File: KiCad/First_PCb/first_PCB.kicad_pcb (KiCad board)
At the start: 2 copper layers, 120 x 120 mm, 41 parts, among them J1 Conn_01x04_Socket, J2 Conn_01x04_Socket, J3 Conn_01x04_Socket, J4 Conn_01x02_Pin, J5 DC-005, U1 MT3608 TYPE-C USB, U2 GH1.25, U3 STEVAL-MKI239A, U4 EGBO UPS, U5 ESP32-DEVKITC-32D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

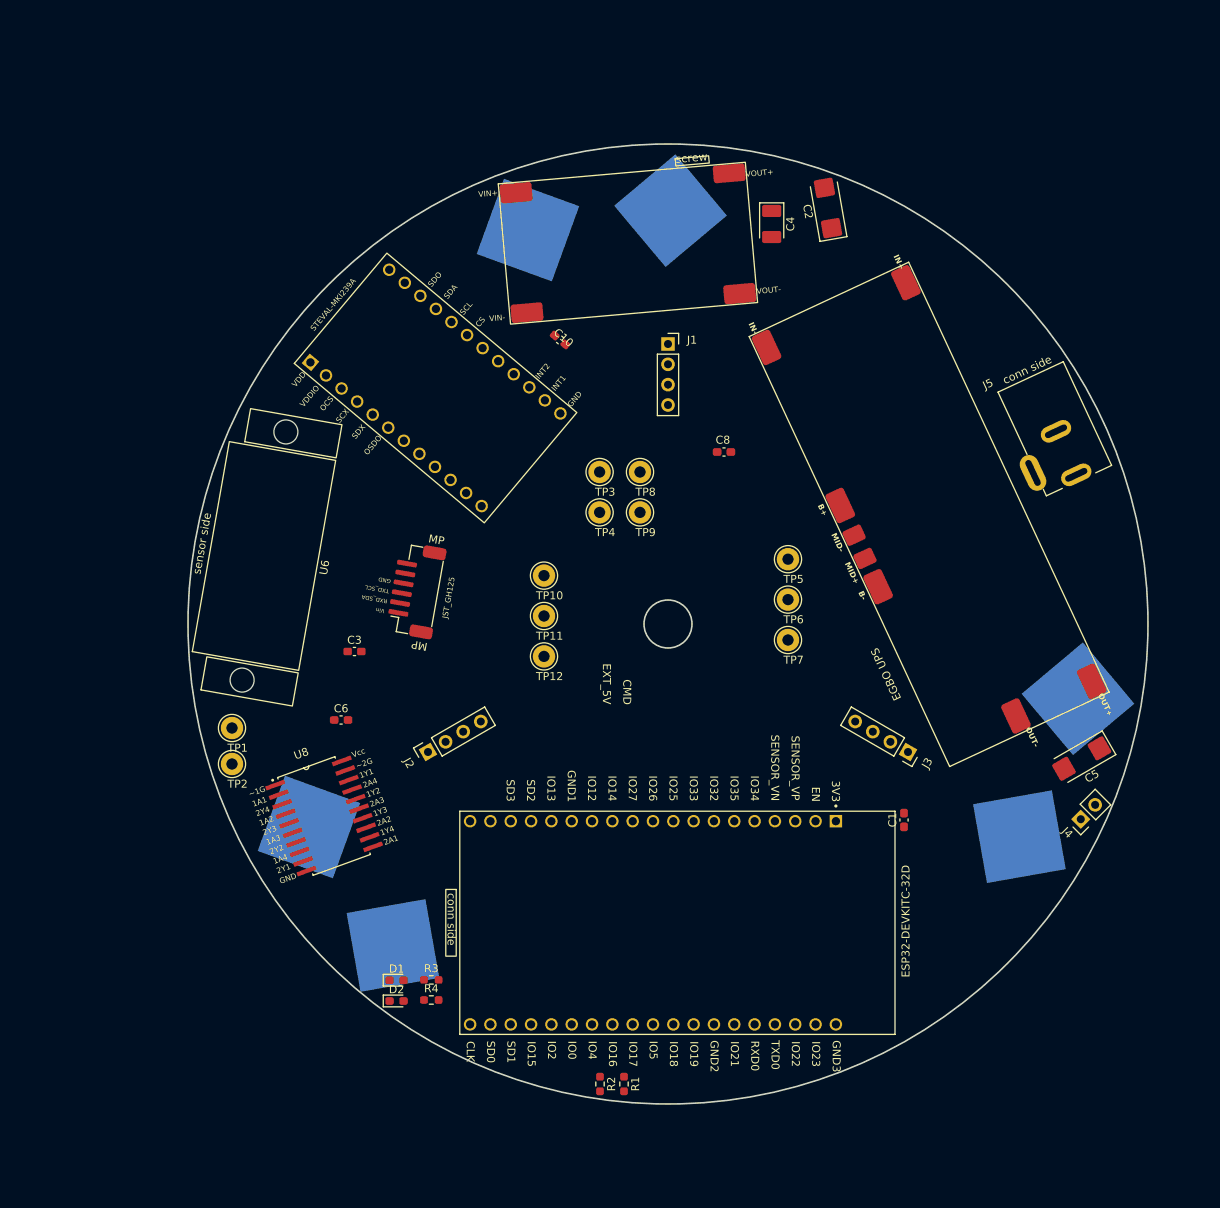
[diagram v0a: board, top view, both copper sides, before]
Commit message: added all the kicad files & gerbers of the first pcb
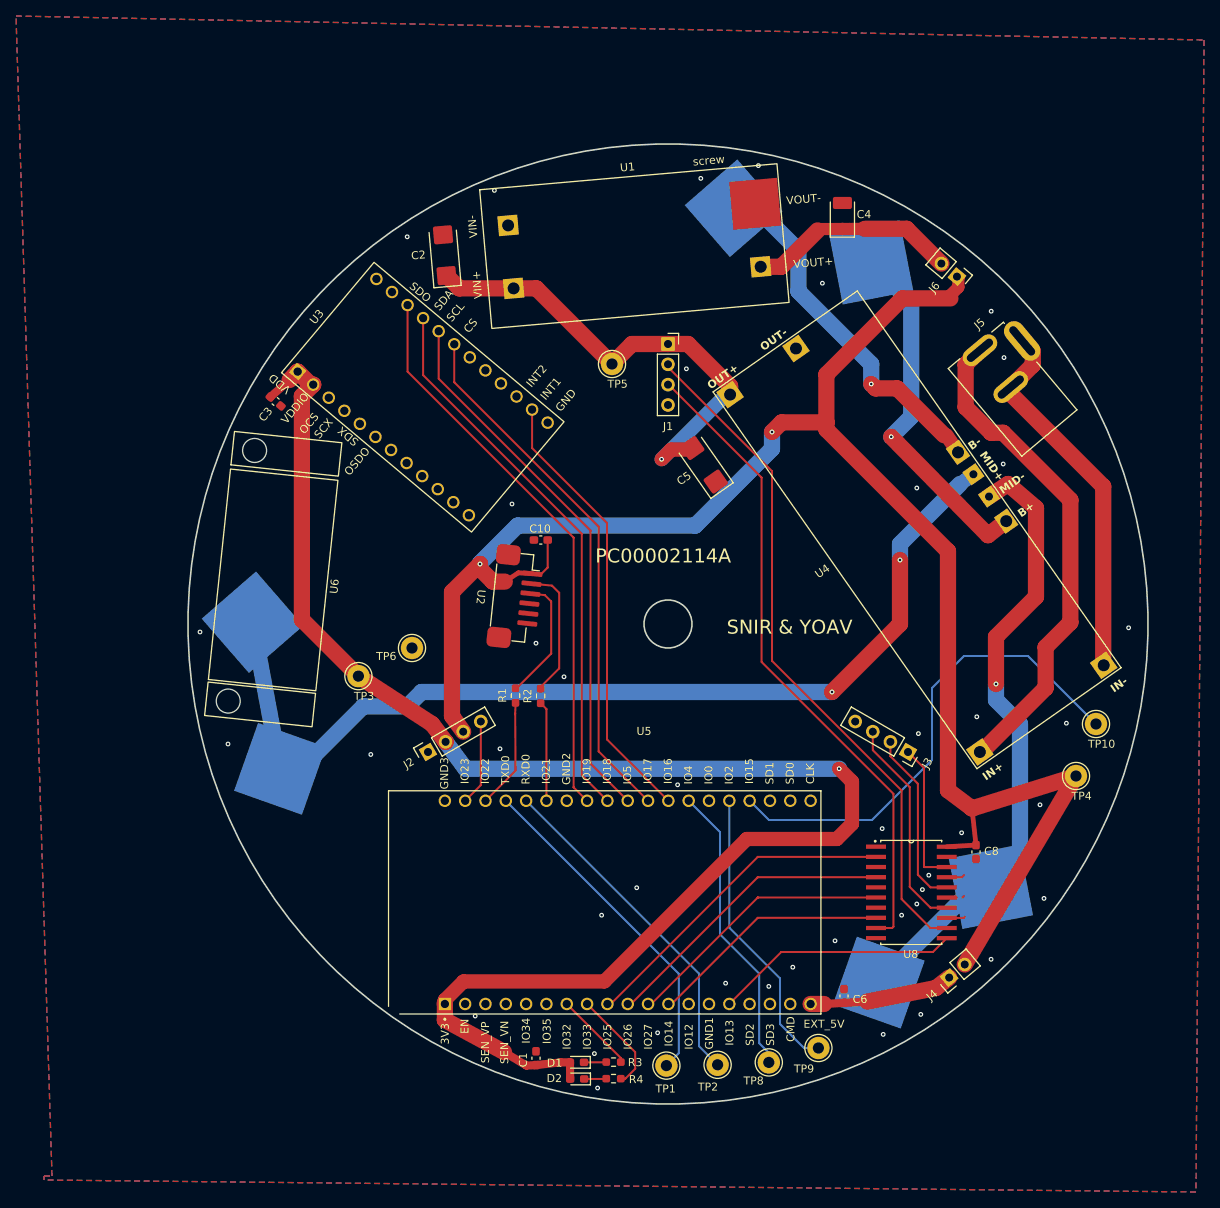
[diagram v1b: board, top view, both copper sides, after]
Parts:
- removed TP11, TP12, TP7: TestPoint, TestPoint:TestPoint_Loop_D2.60mm_Drill1.4mm_Beaded
- added J6: Conn_01x02_Pin, Connector_PinHeader_2.54mm:PinHeader_1x02_P2.54mm_Vertical, F.Cu at (136.1, 56.6)
- U1: value MT3608 TYPE-C USB -> MT3608 - No Connector; footprint footprints:MT3608 Type-C USB -> footprints:MT3608_no_conn_TH
- U4: footprint footprints:PWR_SPLY12V -> footprints:PWR_SPLY12V_TH
- moved TP8 75.5 mm to (112.6, 154.8)
- moved U8 74.0 mm to (130.4, 133.6), turned to 0 degrees
- moved C6 71.7 mm to (122.0, 146.5), turned to 90 degrees
- moved TP10 71.5 mm to (153.5, 112.5)
- moved TP2 71.4 mm to (106.2, 155.1)
- moved TP9 70.6 mm to (118.8, 153.0)
- moved TP1 68.8 mm to (99.8, 155.2)
- moved TP4 68.1 mm to (151.0, 119.0)
- moved C5 59.8 mm to (104.5, 80.1), turned to 125 degrees
- moved C8 59.1 mm to (138.5, 128.5), turned to -90 degrees
- moved C1 54.8 mm to (83.5, 154.3)
- moved R1 50.4 mm to (80.9, 109.0), turned to 90 degrees
- moved R2 49.1 mm to (84.1, 109.0), turned to 90 degrees
- moved C2 48.3 mm to (72.1, 53.9), turned to 95 degrees
- moved TP6 47.4 mm to (68.0, 103.0)
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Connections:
- BT1 pad N: Net-(U4-MID+) -> Net-(U4-B-)
- BT1 pad P: Net-(U4-B+) -> Net-(U4-MID-)
- BT2 pad N: Net-(U4-MID-) -> Net-(U4-MID+)
- BT2 pad P: Net-(U4-MID+) -> Net-(U4-B+)
- BT3 pad N: Net-(U4-B-) -> Net-(U4-MID-)
- BT3 pad P: Net-(U4-MID-) -> Net-(U4-MID+)
- C4 pad 1: +5V -> Net-(J6-Pin_2)
- C6 pad 1: +5V -> Net-(J4-Pin_1)
- J1 pad 1: /Processing/ESP_LEDS_CLK -> +12V
- J1 pad 2: /Processing/ESP_LEDS_SDI1 -> /Processing/ESP_LEDS_SDI4
- J1 pad 3: +3.3V -> /Processing/ESP_LEDS_CLK
- J2 pad 1: /Processing/ESP_2ND_PCB_GPIO4 -> GND
- J2 pad 2: /Processing/ESP_LEDS_SDI2 -> +3.3V
- J2 pad 4: GND -> /Processing/ESP_2ND_PCB_GPIO23
- J3 pad 1: /Processing/ESP_LEDS_SDI4 -> /Processing/ESP_LEDS_SDI1
- J3 pad 2: /Processing/ESP_LEDS_SDI3 -> /Processing/ESP_LEDS_SDI2
- J3 pad 3: +12V -> /Processing/ESP_LEDS_SDI3
- R1 pad 1: Net-(U5-IO17) -> Net-(U5-IO22)
- R1 pad 2: /Processing/ESP_LUNA_UART_TX -> /Processing/ESP_LUNA_UART_RX
- R2 pad 1: Net-(U5-IO16) -> Net-(U5-IO21)
- R2 pad 2: /Processing/ESP_LUNA_UART_RX -> /Processing/ESP_LUNA_UART_TX
- R4 pad 1: /Display/ESP_ST_LED2 -> /Processing/ESP_ST_LED2
- TP10 pad 1: /Processing/ESP_first_PCB_GPIO2 -> /Processing/ESP_TP_GPIO15
- TP8 pad 1: /Test Pins/ESP_first_PCB_GPIO22 -> /Test Pins/ESP_TP_GPIO4
- TP9 pad 1: /Processing/ESP_first_PCB_GPIO15 -> /Processing/ESP_TP_GPIO2
- U1 pad 3: +5V -> Net-(J6-Pin_2)
- U5 pad J2-10: /Processing/ESP_LEDS_SDI4_3.3v -> /Processing/ESP_LEDS_SDI2_3.3v
- U5 pad J2-12: /Processing/ESP_LEDS_SDI2_3.3v -> /Processing/ESP_LEDS_SDI4_3.3v
- U5 pad J2-15: /Processing/ESP_LEDS_SDI1_3.3v -> /Processing/ESP_LEDS_CLK_3.3v
- U5 pad J2-5: /Processing/ESP_first_PCB_GPIO34 -> unconnected-(U5-IO34-PadJ2-5)
- U5 pad J2-6: /Processing/ESP_first_PCB_GPIO35 -> unconnected-(U5-IO35-PadJ2-6)
- U5 pad J2-7: /Processing/JYRO_ESP_INT1 -> /Processing/ESP_ST_LED1
- U5 pad J2-8: /Processing/ESP_ST_LED1 -> /Processing/ESP_ST_LED2
- U5 pad J2-9: /Processing/ESP_LEDS_CLK_3.3v -> /Processing/ESP_LEDS_SDI1_3.3v
- U5 pad J3-10: /Processing/ESP_JYRO_SPI_CS -> /Processing/ESP_JYRO_SPI_CLK
- U5 pad J3-11: Net-(U5-IO17) -> /Processing/ESP_JYRO_SPI_CS
- U5 pad J3-12: Net-(U5-IO16) -> /Processing/JYRO_ESP_INT1
- U5 pad J3-13: /Processing/ESP_2ND_PCB_GPIO4 -> /Test Pins/ESP_TP_GPIO4
- U5 pad J3-15: /Processing/ESP_first_PCB_GPIO2 -> /Processing/ESP_TP_GPIO2
- U5 pad J3-16: /Processing/ESP_first_PCB_GPIO15 -> /Processing/ESP_TP_GPIO15
- U5 pad J3-2: /Processing/ESP_JYRO_SPI_MOSI -> /Processing/ESP_2ND_PCB_GPIO23
- U5 pad J3-3: /Test Pins/ESP_first_PCB_GPIO22 -> Net-(U5-IO22)
- U5 pad J3-6: /Display/ESP_ST_LED2 -> Net-(U5-IO21)
- U5 pad J3-9: /Processing/ESP_JYRO_SPI_CLK -> /Processing/ESP_JYRO_SPI_MOSI
- U8 pad 13: unconnected-(U8-2A2-Pad13) -> GND
- U8 pad 15: unconnected-(U8-2A3-Pad15) -> GND
- U8 pad 17: unconnected-(U8-2A4-Pad17) -> GND
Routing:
- net +5V: track 0.00 -> 222.5 mm, vias 0 -> 2
- net +3.3V: track 0.00 -> 201.4 mm, vias 0 -> 1
- net Net-(U4-MID-): track 0.00 -> 126.3 mm, vias 0 -> 2
- net /Processing/ESP_LEDS_SDI4: track 0.00 -> 87.2 mm
- net /Processing/ESP_LEDS_CLK: track 0.00 -> 81.7 mm
- net Net-(U4-MID+): track 0.00 -> 78.6 mm, vias 0 -> 1
- net /Processing/ESP_JYRO_SPI_MISO: track 0.00 -> 71.4 mm
- net /Processing/ESP_JYRO_SPI_MOSI: track 0.00 -> 69.9 mm
- net /Processing/ESP_JYRO_SPI_CLK: track 0.00 -> 68.5 mm
- net /Processing/ESP_JYRO_SPI_CS: track 0.00 -> 67.1 mm
- net Net-(U4-In+): track 0.00 -> 62.1 mm
- net /Processing/ESP_TP_GPIO15: track 0.00 -> 61.6 mm
- net +12V: track 0.00 -> 60.6 mm, vias 0 -> 1
- net /Processing/JYRO_ESP_INT1: track 0.00 -> 56.0 mm
- net Net-(U4-In-): track 0.00 -> 47.0 mm
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- added copper zone on B.Cu, net GND
- added copper zone on F.Cu, net GND
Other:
- board text added: "0.2540 mm / 0.2540 mm"
- board text added: "0.3000 mm"
- board text added: "1.6002 mm"
- board text added: "120.0025 mm x 120.0025 mm"
- board text added: "2"
- board text added: "BOARD CHARACTERISTICS"
- board text added: "Board Thickness:"
- board text added: "Board overall dimensions:"
- board text added: "Castellated pads:"
- board text added: "Copper Finish:"
- board text added: "Copper Layer Count:"
- board text added: "Edge card connectors:"
- board text added: "Impedance Control:"
- board text added: "Min hole diameter:"
- board text added: "Min track/spacing:"
- board text added: "No"
- board text added: "None"
- board text added: "PC00002114A"
- board text added: "PC00002114A MANUFACTURING NOTES: 1. THIS BOARD IS: 2 LAYERS. 2. THICKNESS 1.6 MM AFTER PLATING. 3. MATERIALS: GLASS EPOXY FR-4 TG170. 4. FINISH H.A.S.L. 5. SOLDER MASK PER IPC-SM 840A, COLOR GREEN. 6. SILK SCREEN: WHITE EPOXY INK. 7. DIAMETER OF OUTER CIRCLE 120 MM. 8. DIAMETER OF INNER CIRCLE 6 MM."
- board text added: "Plated Board Edge:"
- board text added: "SNIR & YOAV"
